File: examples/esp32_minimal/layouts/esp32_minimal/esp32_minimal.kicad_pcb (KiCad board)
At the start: 2 copper layers, 36.2 x 26.8 mm, 20 parts

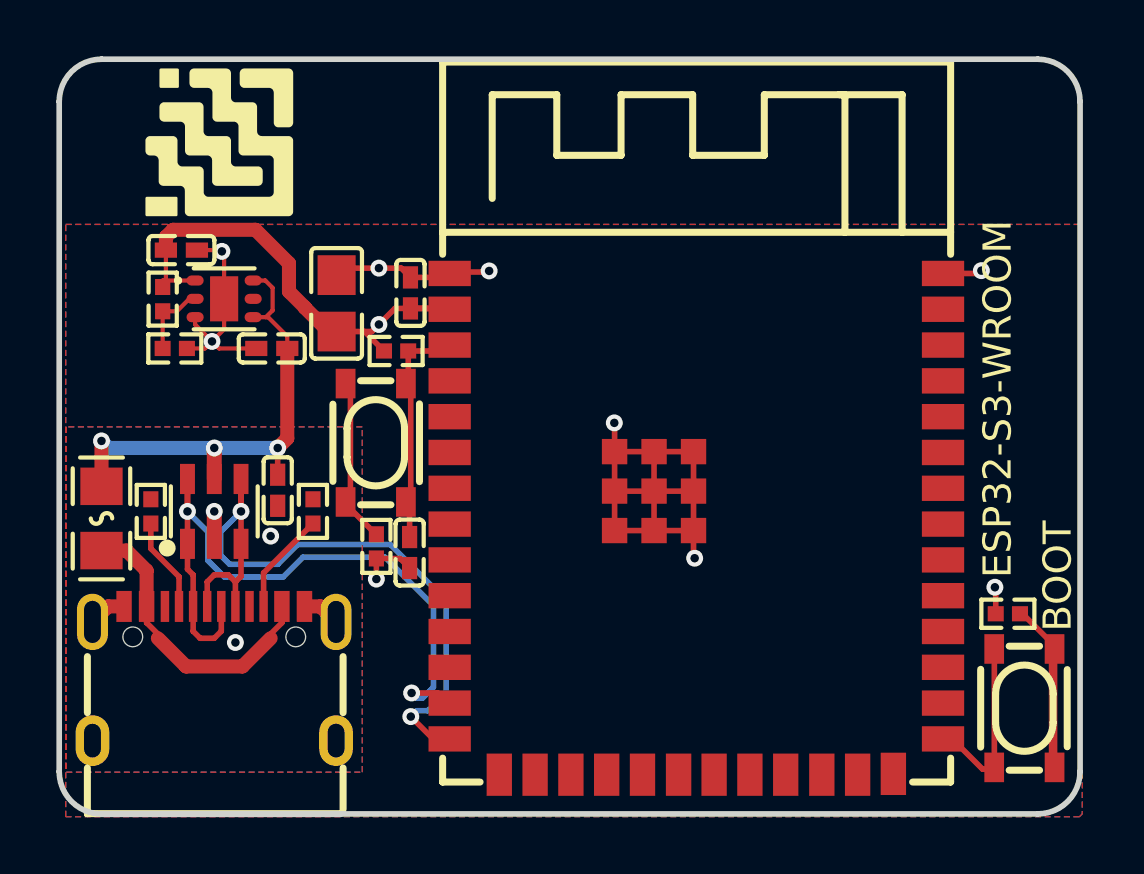
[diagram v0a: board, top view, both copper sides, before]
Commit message: tidy up esp32_minimal layout
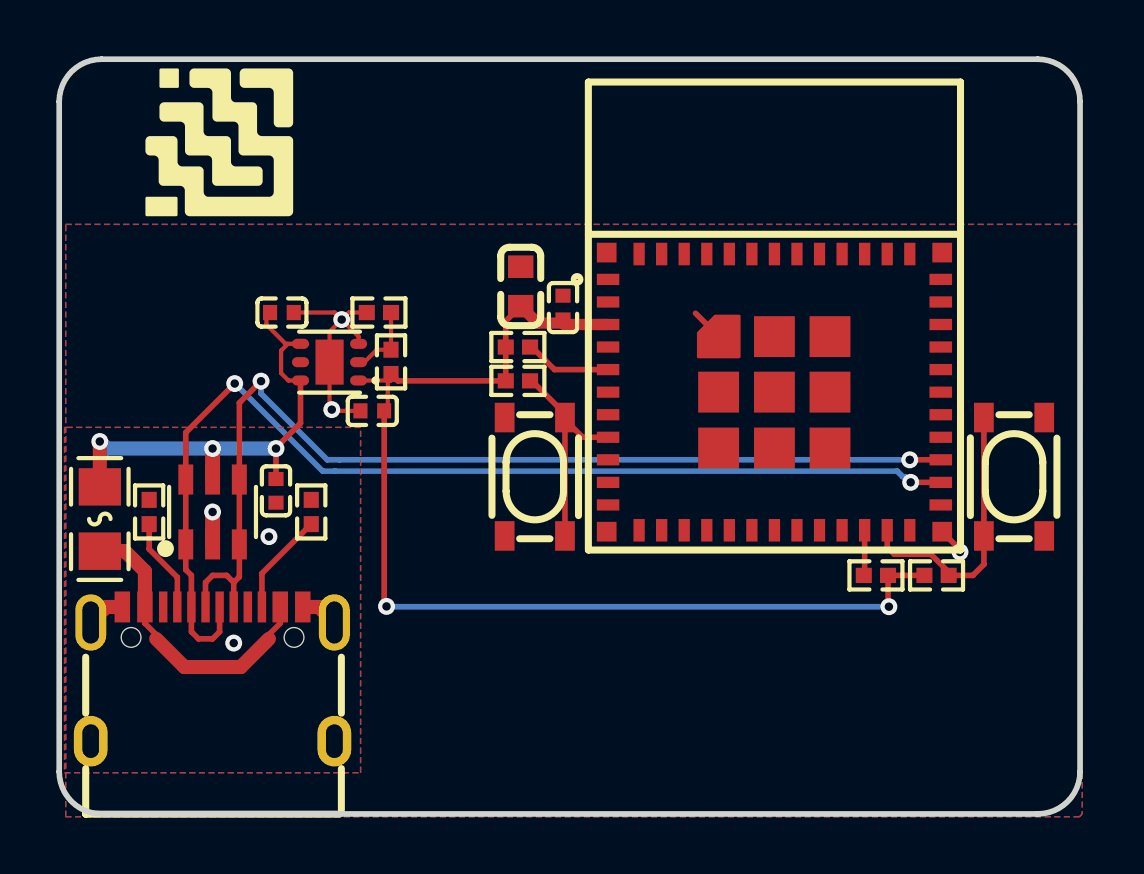
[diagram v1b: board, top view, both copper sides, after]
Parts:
- removed C10: 1µF ±10% 25V X5R, Samsung_Electro_Mechanics_CL05A105KA5NQNC:C0402
- removed C8: 100nF ±10% 16V X7R, Samsung_Electro_Mechanics_CL05B104KO5NNNC:C0402
- removed C9: 22µF ±20% 6.3V X5R, Samsung_Electro_Mechanics_CL21A226MQQNNNE:C0805
- removed U3: , Texas_Instruments_TLV75901PDRVR:WSON-6_L2.0-W2.0-P0.65-TL-EP
- added C4: 100nF ±10% 16V X7R, Samsung_Electro_Mechanics_CL05B104KO5NNNC:C0402, F.Cu at (147.1, 119.8)
- added C5: 100nF ±10% 16V X7R, Samsung_Electro_Mechanics_CL05B104KO5NNNC:C0402, F.Cu at (136.9, 126.3)
- added R8: 5.1kΩ ±1% 62.5mW, UNI_ROYAL_0402WGF5101TCE:R0402, F.Cu at (138.2, 127.0)
- added U1: , Texas_Instruments_TLV75901PDRVR:WSON-6_L2.0-W2.0-P0.65-TL-EP, F.Cu at (138.8, 121.7)
- C3: value 100nF ±10% 16V X7R -> 22µF ±20% 6.3V X5R; footprint Samsung_Electro_Mechanics_CL05B104KO5NNNC:C0402 -> Samsung_Electro_Mechanics_CL10A226MQ8NRNC:C0603
- R2: value 100Ω ±1% 62.5mW -> 47kΩ ±1% 62.5mW; footprint UNI_ROYAL_0402WGF1000TCE:R0402 -> UNI_ROYAL_0402WGF4702TCE:R0402
- R4: value 100Ω ±1% 62.5mW -> 10kΩ ±1% 62.5mW; footprint UNI_ROYAL_0402WGF1000TCE:R0402 -> UNI_ROYAL_0402WGF1002TCE:R0402
- R5: value 47kΩ ±1% 62.5mW -> 5.1kΩ ±1% 62.5mW; footprint UNI_ROYAL_0402WGF4702TCE:R0402 -> UNI_ROYAL_0402WGF5101TCE:R0402
- R6: value 5.1kΩ ±1% 62.5mW -> 10kΩ ±1% 62.5mW; footprint UNI_ROYAL_0402WGF5101TCE:R0402 -> UNI_ROYAL_0402WGF1002TCE:R0402
- U2: footprint Espressif_Systems_ESP32_S3_WROOM_1_N8R8:WIRELM-SMD_ESP32-S3-WROOM-1 -> Espressif_Systems_ESP32_C3_MINI_1_N4:WIFIM-SMD_ESP32-C3-MINI-1
- moved R5 29.1 mm to (160.4, 129.3), turned to 0 degrees
- moved R2 23.6 mm to (141.0, 121.7), turned to 90 degrees
- moved R4 17.7 mm to (158.2, 129.3), turned to 0 degrees
- moved R6 13.8 mm to (145.5, 122.4), turned to 0 degrees
- moved C3 11.3 mm to (145.6, 119.0), turned to 90 degrees
- moved C2 8.85 mm to (140.4, 123.4), turned to 180 degrees
- moved SW1 8.22 mm to (163.1, 125.8)
- moved R1 7.35 mm to (140.6, 119.9), turned to 180 degrees
- moved R7 5.81 mm to (132.4, 127.0)
- moved SW2 5.77 mm to (146.1, 125.8)
- moved U2 5.44 mm to (154.6, 122.8)
- moved R3 4.32 mm to (145.5, 121.2)
- moved C1 1.32 mm to (137.2, 119.9), turned to 0 degrees
- moved USB1 0.06 mm to (134.7, 132.8)
- moved D1 0.06 mm to (134.7, 127.0)
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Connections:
- net CTS renamed esp32_c3-net-11
- net IO35 renamed esp32_c3-net-3
- net IO36 renamed esp32_c3-net-4
- net IO47 renamed esp32_c3-net-0
- net IO48 renamed esp32_c3-net-1
- net IO9 renamed esp32_c3-net-13
- net SDA renamed esp32_c3-net-10
- net TCK renamed esp32_c3-net-5
- net TDI renamed esp32_c3-net-7
- net TDO renamed esp32_c3-net-6
- net TMS renamed esp32_c3-net-8
- net i2s[0]-SD renamed esp32_c3-net-9
- net i2s[0]-WS renamed esp32_c3-net-12
- net i2s[1]-SD renamed SCK
- net i2s[1]-WS renamed WS
- net spi[2]-MISO renamed data_0
- net spi[2]-MOSI renamed data_2
- net spi_cs[2]-line renamed data_3
- net uart[1]-MISO renamed esp32_c3-net-2
- C3 pad 1: power_in-VCC -> power-VCC
- R2 pad 1: button-input-input-0 -> power-VCC
- R2 pad 2: GND -> VDIV_OUTPUT
- R3 pad 1: output-output -> data_1
- R4 pad 1: button-input-input-1 -> MISO
- R4 pad 2: GND -> power-VCC
- R5 pad 2: VDIV_OUTPUT -> output
- R6 pad 1: cc[0]-line -> power-VCC
- R6 pad 2: GND -> N_TRST
- R7 pad 1: cc[1]-line -> cc[0]-line
- SW1 pad 1: button-input-input-0 -> GND
- SW1 pad 2: button-input-input-0 -> GND
- SW1 pad 3: gpios[0]-output -> output
- SW1 pad 4: gpios[0]-output -> output
- SW2 pad 1: button-input-input-1 -> GND
- SW2 pad 2: button-input-input-1 -> GND
- SW2 pad 3: output-output -> N_TRST
- SW2 pad 4: output-output -> N_TRST
- U2 pad 11: RX -> GND
- U2 pad 13: USB_D_N -> SD
- U2 pad 14: USB_D_P -> GND
- U2 pad 16: IO46 -> SCLK
- U2 pad 2: power-VCC -> GND
- U2 pad 20: SCLK -> SCL
- U2 pad 22: spi_cs[3]-SCL -> MISO
- U2 pad 23: TX -> output
- U2 pad 26: IO45 -> USB_D_N
- U2 pad 27: gpios[0]-output -> USB_D_P
- U2 pad 3: output-output -> power-VCC
- U2 pad 30: IO37 -> RX
- U2 pad 31: IO38 -> TX
- U2 pad 36: RXD0 -> GND
- U2 pad 37: TXD0 -> GND
- U2 pad 38: i2s[0]-SCK -> GND
- U2 pad 39: i2c[0]-SCL -> GND
- U2 pad 5: i2s[1]-SCK -> data_1
- U2 pad 8: uart[0]-MOSI -> N_TRST
- USB1 pad : net -> (no net)
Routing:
- net GND: track 41.0 -> 14.1 mm, vias 12 -> 6
- net power-VCC: track 18.1 -> 40.4 mm, vias 1 -> 2
- net USB_D_N: track 25.3 -> 38.2 mm
- net USB_D_P: track 25.4 -> 36.0 mm
- net button-input-input-0: track 10.3 -> 0.00 mm
- net output: track 0.00 -> 9.89 mm
- net output-output: track 8.21 -> 0.00 mm
- net N_TRST: track 0.00 -> 7.92 mm
- net gpios[0]-output: track 6.46 -> 0.00 mm
- net button-input-input-1: track 5.75 -> 0.00 mm
- net data_1: track 0.00 -> 3.10 mm
- net MISO: track 0.00 -> 1.61 mm
- net power_in-VCC: track 17.5 -> 16.6 mm
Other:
- board text removed: "BOOT"
- board text removed: "ESP32-S3-WROOM"

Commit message: Revert "tidy up esp32_minimal layout"
This reverts commit 4b4c020cd5ce75f8a8c2c869c7ee81213b903a87.
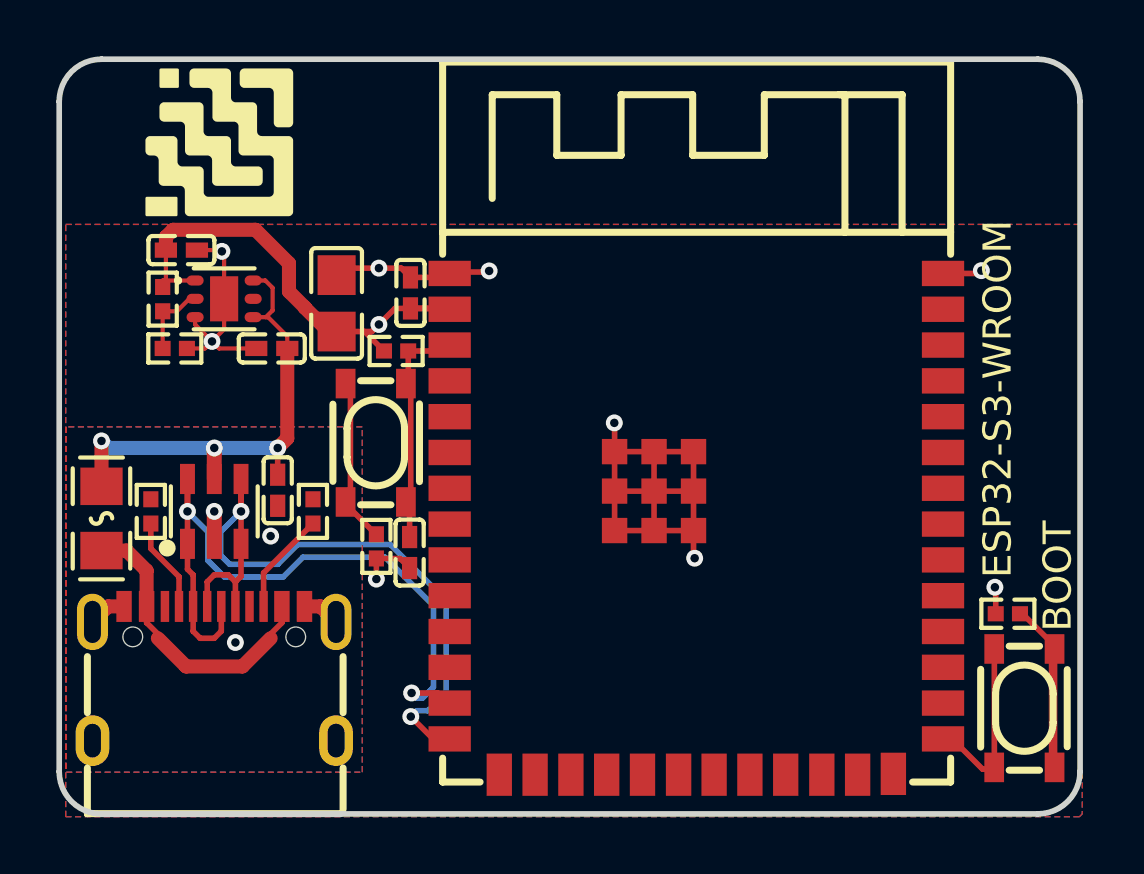
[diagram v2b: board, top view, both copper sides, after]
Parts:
- removed C4, C5: 100nF ±10% 16V X7R, Samsung_Electro_Mechanics_CL05B104KO5NNNC:C0402
- removed R8: 5.1kΩ ±1% 62.5mW, UNI_ROYAL_0402WGF5101TCE:R0402
- removed U1: , Texas_Instruments_TLV75901PDRVR:WSON-6_L2.0-W2.0-P0.65-TL-EP
- added C10: 1µF ±10% 25V X5R, Samsung_Electro_Mechanics_CL05A105KA5NQNC:C0402, F.Cu at (141.7, 128.5)
- added C8: 100nF ±10% 16V X7R, Samsung_Electro_Mechanics_CL05B104KO5NNNC:C0402, F.Cu at (141.7, 119.2)
- added C9: 22µF ±20% 6.3V X5R, Samsung_Electro_Mechanics_CL21A226MQQNNNE:C0805, F.Cu at (139.1, 119.6)
- added U3: , Texas_Instruments_TLV75901PDRVR:WSON-6_L2.0-W2.0-P0.65-TL-EP, F.Cu at (135.1, 119.5)
- C3: value 22µF ±20% 6.3V X5R -> 100nF ±10% 16V X7R; footprint Samsung_Electro_Mechanics_CL10A226MQ8NRNC:C0603 -> Samsung_Electro_Mechanics_CL05B104KO5NNNC:C0402
- R2: value 47kΩ ±1% 62.5mW -> 100Ω ±1% 62.5mW; footprint UNI_ROYAL_0402WGF4702TCE:R0402 -> UNI_ROYAL_0402WGF1000TCE:R0402
- R4: value 10kΩ ±1% 62.5mW -> 100Ω ±1% 62.5mW; footprint UNI_ROYAL_0402WGF1002TCE:R0402 -> UNI_ROYAL_0402WGF1000TCE:R0402
- R5: value 5.1kΩ ±1% 62.5mW -> 47kΩ ±1% 62.5mW; footprint UNI_ROYAL_0402WGF5101TCE:R0402 -> UNI_ROYAL_0402WGF4702TCE:R0402
- R6: value 10kΩ ±1% 62.5mW -> 5.1kΩ ±1% 62.5mW; footprint UNI_ROYAL_0402WGF1002TCE:R0402 -> UNI_ROYAL_0402WGF5101TCE:R0402
- U2: footprint Espressif_Systems_ESP32_C3_MINI_1_N4:WIFIM-SMD_ESP32-C3-MINI-1 -> Espressif_Systems_ESP32_S3_WROOM_1_N8R8:WIRELM-SMD_ESP32-S3-WROOM-1
- moved R5 29.1 mm to (132.9, 119.5), turned to -90 degrees
- moved R2 23.6 mm to (162.9, 130.6), turned to 180 degrees
- moved R4 17.7 mm to (140.5, 128.2), turned to -90 degrees
- moved R6 13.8 mm to (132.5, 127.0), turned to 90 degrees
- moved C3 11.3 mm to (137.0, 126.2), turned to -90 degrees
- moved C2 8.85 mm to (133.6, 117.7), turned to 0 degrees
- moved SW1 8.22 mm to (163.5, 134.0)
- moved R1 7.35 mm to (133.3, 121.2), turned to 0 degrees
- moved R7 5.81 mm to (138.2, 127.0)
- moved SW2 5.77 mm to (140.5, 124.6)
- moved U2 5.44 mm to (151.8, 127.5)
- moved R3 4.32 mm to (141.2, 121.3)
- moved C1 1.32 mm to (136.8, 121.2), turned to 180 degrees
- moved USB1 0.06 mm to (134.8, 132.8)
- moved D1 0.06 mm to (134.8, 127.0)
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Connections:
- net SCK renamed i2s[1]-SD
- net WS renamed i2s[1]-WS
- net data_0 renamed spi[2]-MISO
- net data_2 renamed spi[2]-MOSI
- net data_3 renamed spi_cs[2]-line
- net esp32_c3-net-0 renamed IO47
- net esp32_c3-net-1 renamed IO48
- net esp32_c3-net-10 renamed SDA
- net esp32_c3-net-11 renamed CTS
- net esp32_c3-net-12 renamed i2s[0]-WS
- net esp32_c3-net-13 renamed IO9
- net esp32_c3-net-2 renamed uart[1]-MISO
- net esp32_c3-net-3 renamed IO35
- net esp32_c3-net-4 renamed IO36
- net esp32_c3-net-5 renamed TCK
- net esp32_c3-net-6 renamed TDO
- net esp32_c3-net-7 renamed TDI
- net esp32_c3-net-8 renamed TMS
- net esp32_c3-net-9 renamed i2s[0]-SD
- C3 pad 1: power-VCC -> power_in-VCC
- R2 pad 1: power-VCC -> button-input-input-0
- R2 pad 2: VDIV_OUTPUT -> GND
- R3 pad 1: data_1 -> output-output
- R4 pad 1: MISO -> button-input-input-1
- R4 pad 2: power-VCC -> GND
- R5 pad 2: output -> VDIV_OUTPUT
- R6 pad 1: power-VCC -> cc[0]-line
- R6 pad 2: N_TRST -> GND
- R7 pad 1: cc[0]-line -> cc[1]-line
- SW1 pad 1: GND -> button-input-input-0
- SW1 pad 2: GND -> button-input-input-0
- SW1 pad 3: output -> gpios[0]-output
- SW1 pad 4: output -> gpios[0]-output
- SW2 pad 1: GND -> button-input-input-1
- SW2 pad 2: GND -> button-input-input-1
- SW2 pad 3: N_TRST -> output-output
- SW2 pad 4: N_TRST -> output-output
- U2 pad 11: GND -> RX
- U2 pad 13: SD -> USB_D_N
- U2 pad 14: GND -> USB_D_P
- U2 pad 16: SCLK -> IO46
- U2 pad 2: GND -> power-VCC
- U2 pad 20: SCL -> SCLK
- U2 pad 22: MISO -> spi_cs[3]-SCL
- U2 pad 23: output -> TX
- U2 pad 26: USB_D_N -> IO45
- U2 pad 27: USB_D_P -> gpios[0]-output
- U2 pad 3: power-VCC -> output-output
- U2 pad 30: RX -> IO37
- U2 pad 31: TX -> IO38
- U2 pad 36: GND -> RXD0
- U2 pad 37: GND -> TXD0
- U2 pad 38: GND -> i2s[0]-SCK
- U2 pad 39: GND -> i2c[0]-SCL
- U2 pad 5: data_1 -> i2s[1]-SCK
- U2 pad 8: N_TRST -> uart[0]-MOSI
- USB1 pad : (no net) -> net
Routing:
- net GND: track 14.1 -> 41.0 mm, vias 6 -> 12
- net power-VCC: track 40.4 -> 18.1 mm, vias 2 -> 1
- net USB_D_N: track 38.2 -> 25.3 mm
- net USB_D_P: track 36.0 -> 25.4 mm
- net button-input-input-0: track 0.00 -> 10.3 mm
- net output: track 9.89 -> 0.00 mm
- net output-output: track 0.00 -> 8.21 mm
- net N_TRST: track 7.92 -> 0.00 mm
- net gpios[0]-output: track 0.00 -> 6.46 mm
- net button-input-input-1: track 0.00 -> 5.75 mm
- net data_1: track 3.10 -> 0.00 mm
- net MISO: track 1.61 -> 0.00 mm
- net power_in-VCC: track 16.6 -> 17.5 mm
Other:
- board text added: "BOOT"
- board text added: "ESP32-S3-WROOM"

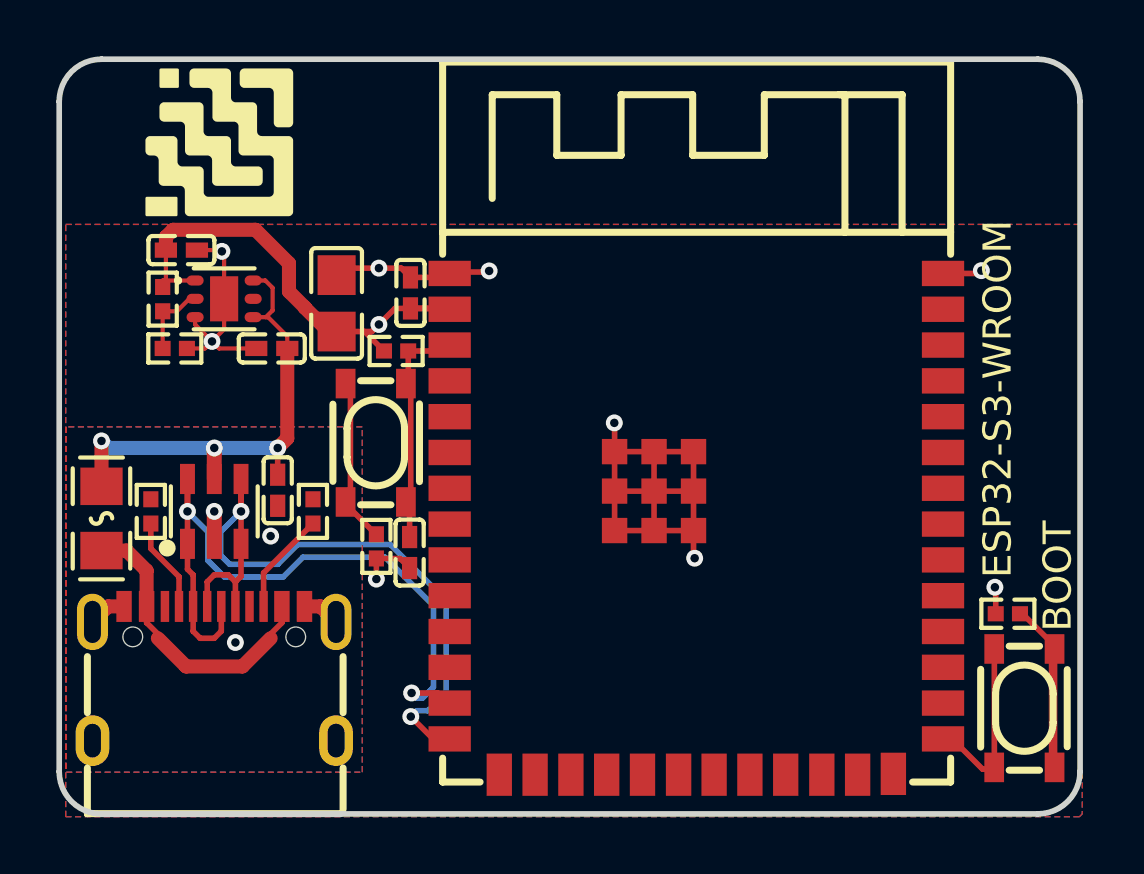
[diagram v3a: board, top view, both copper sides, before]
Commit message: layout_viewer: stabilize pad annotations and improve text rendering
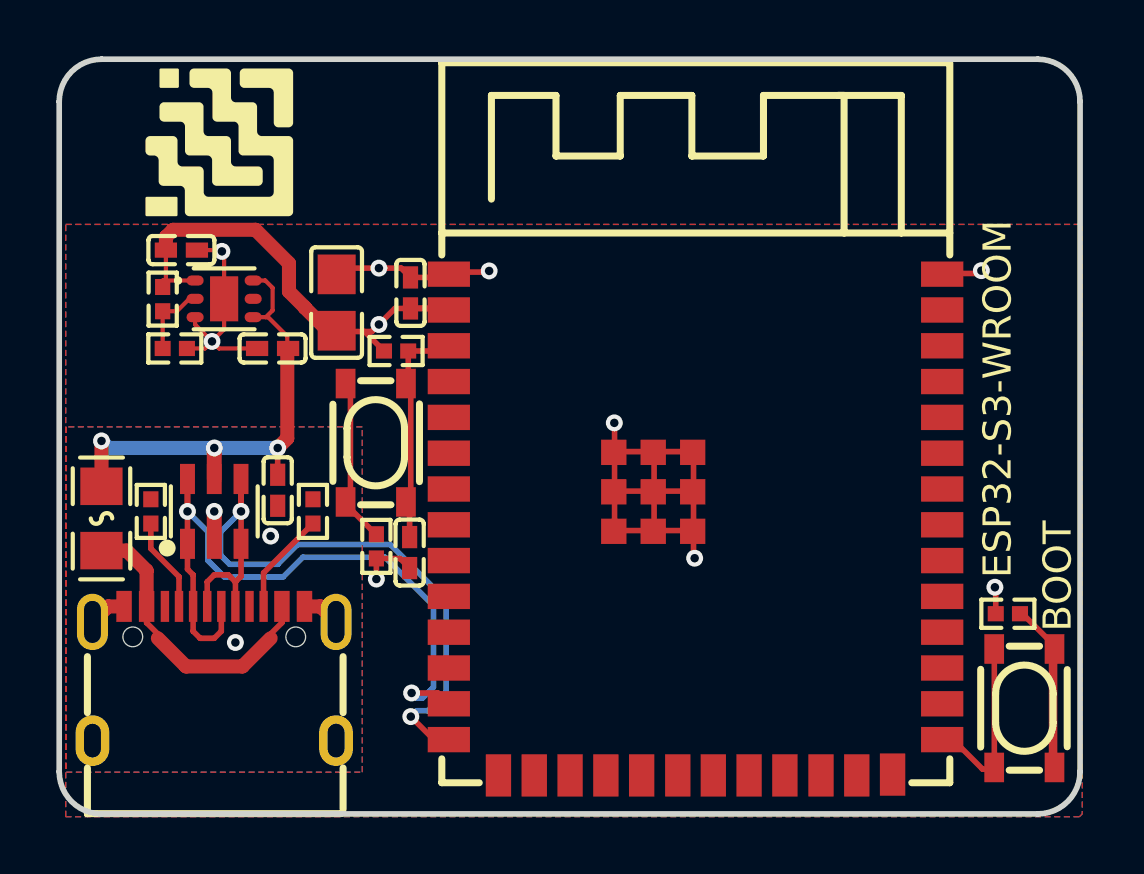
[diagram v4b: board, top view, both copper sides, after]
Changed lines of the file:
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@@
 	(footprint "Samsung_Electro_Mechanics_CL05A105KA5NQNC:C0402"
 		(layer "F.Cu")
-		(at 136.79 121.22 180)
+		(at 136.8182922 121.22 180)
 		(property "Reference" "C1"
 			(at 0 -4 180)
@@
 	(footprint "Samsung_Electro_Mechanics_CL21A226MQQNNNE:C0805"
 		(layer "F.Cu")
-		(at 139.09 119.62 90)
+		(at 139.09 119.5917078 90)
 		(property "Reference" "C9"
 			(at 0 -4 90)
@@
 	(footprint "Espressif_Systems_ESP32_S3_WROOM_1_N8R8:WIRELM-SMD_ESP32-S3-WROOM-1"
 		(layer "F.Cu")
-		(at 151.85 127.45 0)
+		(at 151.8208462 127.4748432 0)
 		(property "Reference" "U2"
 			(at 0 -12.89 0)
